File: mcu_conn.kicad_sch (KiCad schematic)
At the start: 36 parts, among them J11 MD_MCU_PU_EN, J9 MD_MCU_EN, Q6 FDV305N, U2 Teensy4.1, U3 INA190A5IDDFR, U4 INA190A5IDDFR

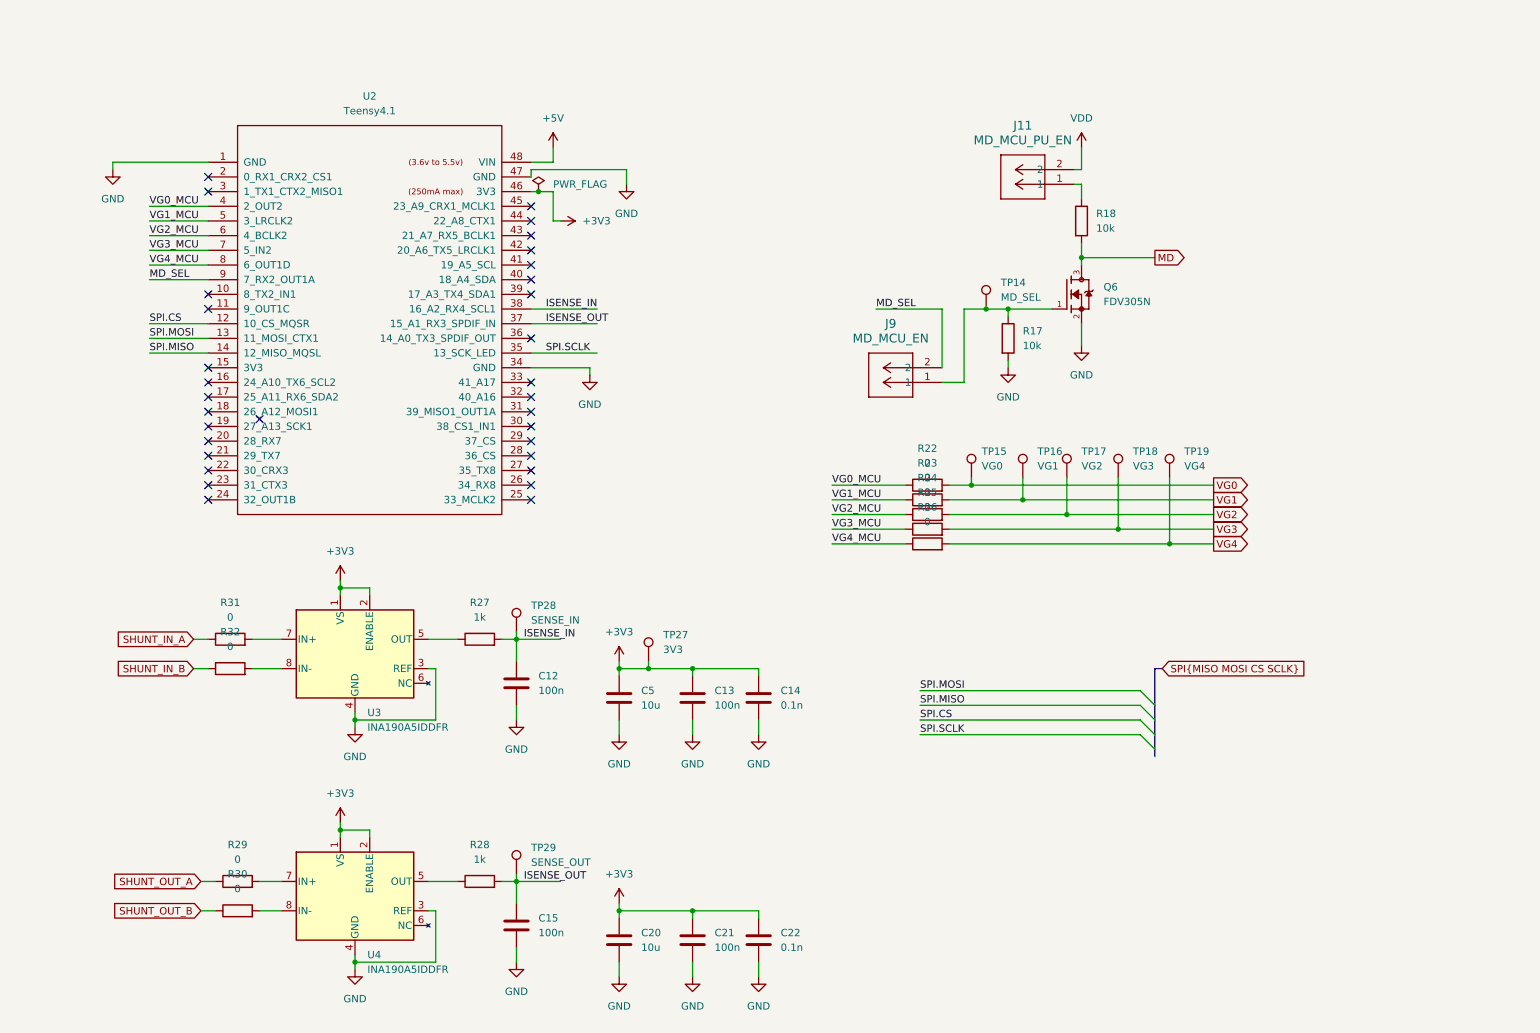
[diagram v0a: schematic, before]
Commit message: Rearrange the MCU sheet and add section titles
Symbols, wires and labels on the MCU sheet moved, and three text notes were
added (MCU, ISENSE AMPS, CONNECTORS). One text position moved on the top
sheet. A netlist export shows the same 105 parts and 79 nets as c5a823f,
with every pin on the same net.
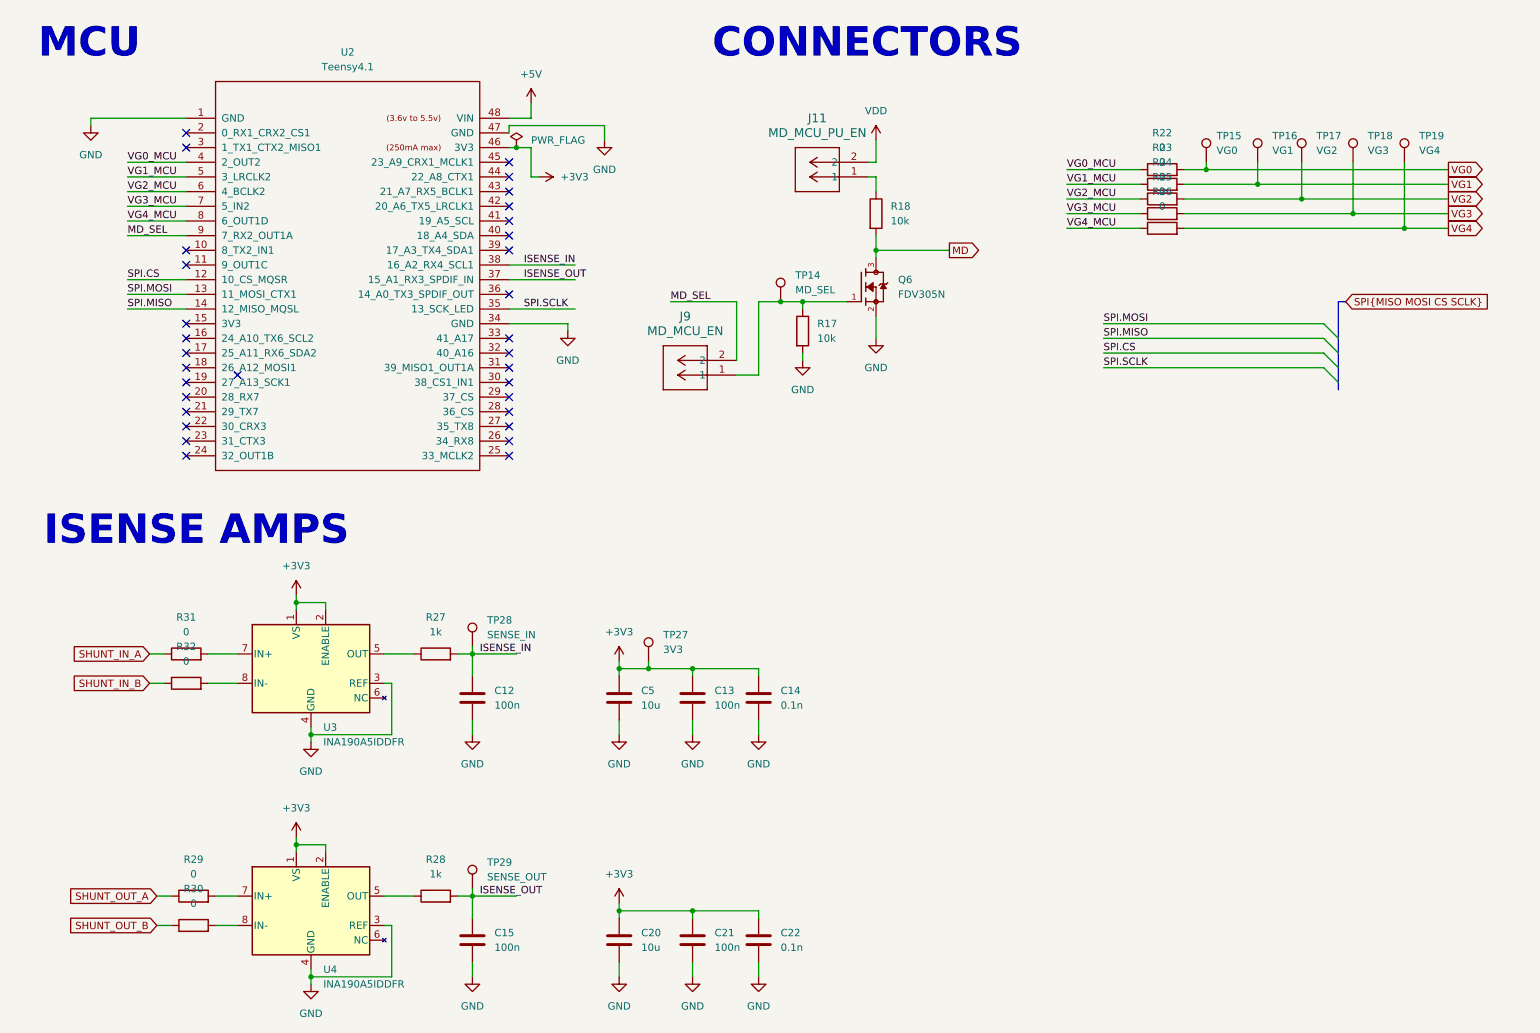
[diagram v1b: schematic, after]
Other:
- note added: "CONNECTORS"
- note added: "ISENSE AMPS"
- note added: "MCU"
- moved on the sheet: C12, C15, J11, J9, Q6, R17, R18, R22, R23, R24, R25, R26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

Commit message: Add the title block to the MCU and temperature sheets
Both sub-sheets now carry the same title, date, revision and four author
names as the top sheet. No parts or nets change.
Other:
- title: (none) -> EE372 LDO bringup board
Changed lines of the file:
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@@
 	(generator_version "10.0")
 	(paper "A4")
+	(title_block
+		(title "EE372 LDO bringup board")
+		(date "2026-08-02")
+		(rev "0")
+		(comment 1 "Luke Qiao")
+		(comment 2 "Spencer Wallace")
+		(comment 3 "Luis Sanchez")
+		(comment 4 "Caleb Ketchum")
+	)
 	(text "CONNECTORS"
 		(exclude_from_sim no)

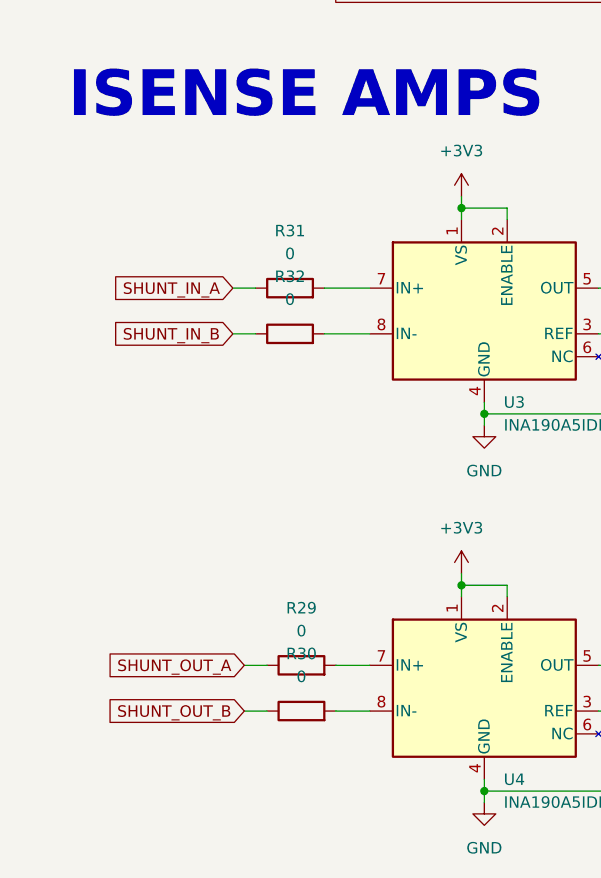
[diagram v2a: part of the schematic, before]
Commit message: Add input filters to both current-sense amplifiers and rework the buffer power
- R29 to R32, in series with the INA190 inputs, change from 0 ohm to 100 ohm,
  and C24 and C25 (100n) go across each amplifier's IN+ and IN-. With the
  100 ohm resistors that is an 8 kHz differential filter on each.
- Buffer sheet. JP4 BUF_EN (2-pin header) replaces J14 between +5V and the
  BUF634A's V+. C23 becomes the 10u 1206 KEMET part, now from V+ to GND. The
  buffer's labels are global now, and R16 joins the buffer output to the VDD
  side of R4 (SHUNT_IN_A).
- One stub wire and its junction removed on the top sheet.

The netlist goes from 113 parts and 85 nets to 115 parts and 84 nets. ERC
shows 1 error, U5's V+ not driven behind JP4, left for the buffer rework along
with V- on GND and five parts that point at the demo board's libraries.
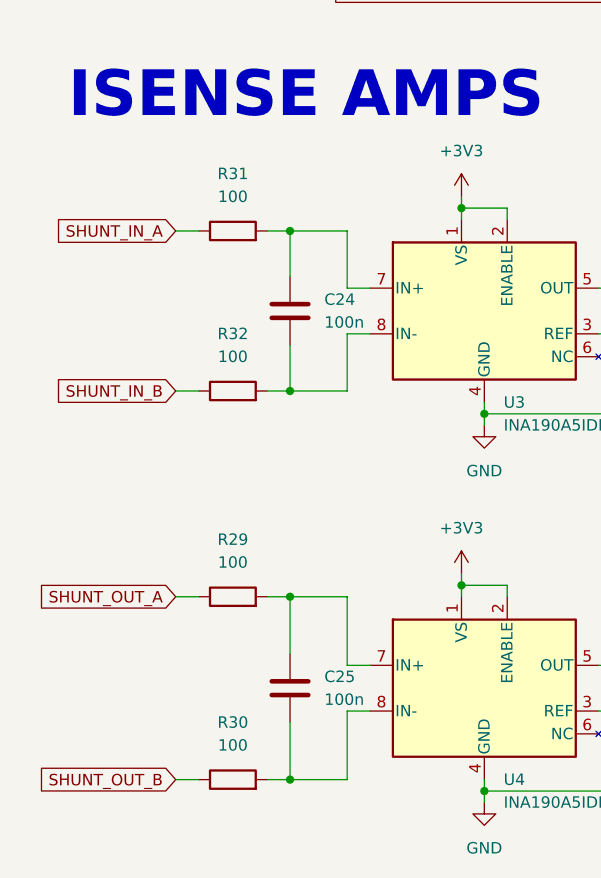
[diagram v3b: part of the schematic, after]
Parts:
- added C24, C25: 100n, Capacitor_SMD:C_0805_2012Metric_Pad1.18x1.45mm_HandSolder, symbol Device:C
- R29, R30, R31, R32: value 0 -> 100; Distributer Link 1 https://www.digikey.com/en/products/detail/vishay-dale/CRCW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 -> https://www.digikey.com/en/products/detail/yageo/RC0805FR-0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; Manufacturer Vishay Dale -> YAGEO; Manufacturer Part Number CRCW08050000Z0EAHP -> RC0805FR-07100RL
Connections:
- net at R31.2, U3.7 (IN+): now also C24.1
- net at R32.2, U3.8 (IN-): now also C24.2
- net at R29.2, U4.7 (IN+): now also C25.1
- net at R30.2, U4.8 (IN-): now also C25.2
